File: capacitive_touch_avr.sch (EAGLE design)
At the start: 11 parts, among them J2 JACK-2.1MM

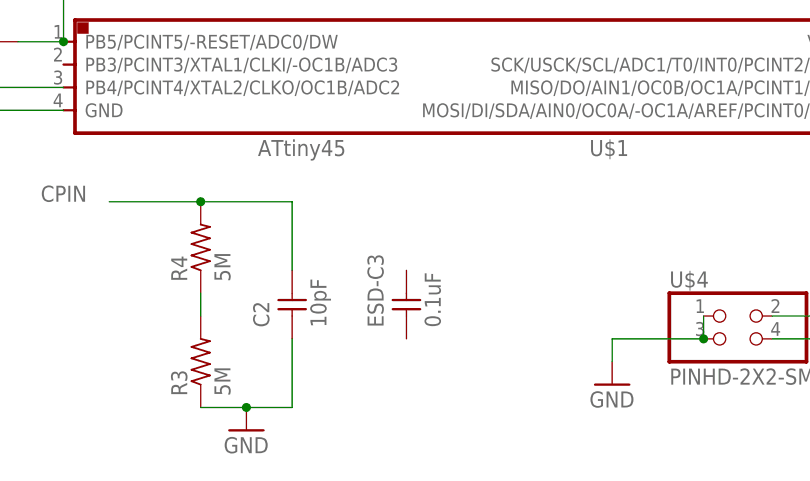
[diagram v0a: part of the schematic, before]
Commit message: Version 2.0 isolate signals from sensor pin + pad design Missing ESD shield + Mounting holes
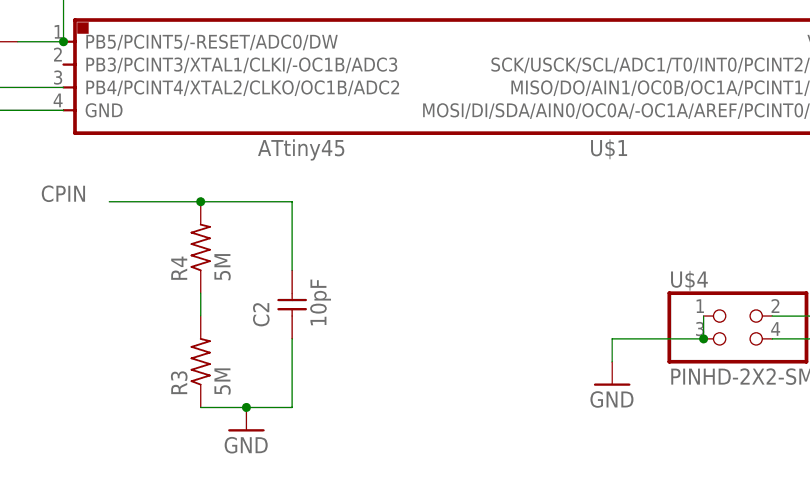
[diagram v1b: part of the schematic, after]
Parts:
- removed ESD-C3: 0.1uF, fab:CAP-UNPOLARIZEDFAB
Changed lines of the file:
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@@
 <part name="P+7" library="supply1" library_urn="urn:adsk.eagle:library:371" deviceset="VCC" device=""/>
 <part name="J2" library="fab" deviceset="JACK-2.1MM" device=""/>
-<part name="ESD-C3" library="fab" deviceset="CAP-UNPOLARIZED" device="FAB" value="0.1uF"/>
 </parts>
 <sheets>
@@
 <instance part="P+7" gate="VCC" x="25.4" y="58.42" rot="R180"/>
 <instance part="J2" gate="G$1" x="27.94" y="73.66" rot="R90"/>
-<instance part="ESD-C3" gate="&gt;NAME" x="53.34" y="22.86" rot="R90"/>
 </instances>
 <busses>

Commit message: Version 1. Touch pad + full wiring
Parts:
- added ESD-C3: 0.1uF, fab:CAP-UNPOLARIZEDFAB
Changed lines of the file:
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@@
 <part name="P+7" library="supply1" library_urn="urn:adsk.eagle:library:371" deviceset="VCC" device=""/>
 <part name="J2" library="fab" deviceset="JACK-2.1MM" device=""/>
+<part name="ESD-C3" library="fab" deviceset="CAP-UNPOLARIZED" device="FAB" value="0.1uF"/>
 </parts>
 <sheets>
@@
 <instance part="P+7" gate="VCC" x="25.4" y="58.42" rot="R180"/>
 <instance part="J2" gate="G$1" x="27.94" y="73.66" rot="R90"/>
+<instance part="ESD-C3" gate="&gt;NAME" x="53.34" y="22.86" rot="R90"/>
 </instances>
 <busses>
